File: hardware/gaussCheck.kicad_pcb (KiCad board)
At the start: 2 copper layers, 28 x 94.7 mm, 42 parts, among them J1 USB_C_Receptacle_USB2.0, J2 SWD, SW1 PTS810, SW2 CK KSC2, SW3 CK KSC2, SW4 CK KSC2, U1 TLV493D, U2 VIM-878-DP, U3 ATSAML22N18A-AUT, U4 TPS613221ADBV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

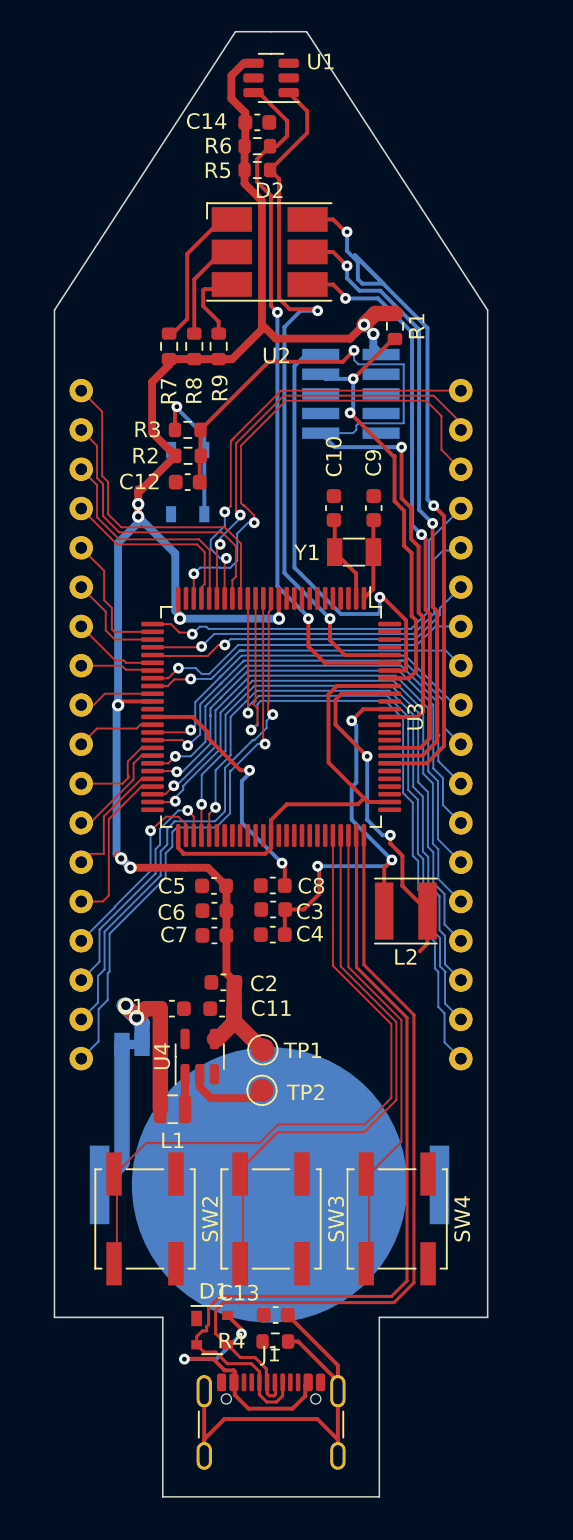
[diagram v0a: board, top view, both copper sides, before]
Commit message: Turned MCU by 45degress and rerouted
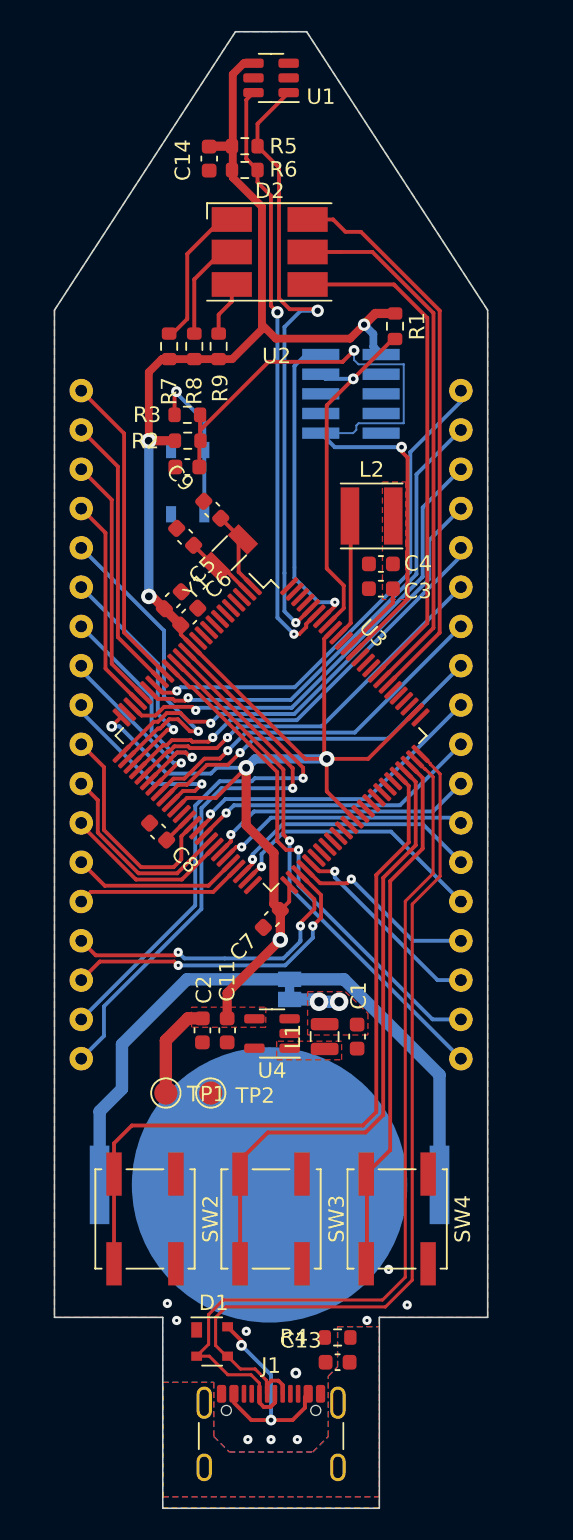
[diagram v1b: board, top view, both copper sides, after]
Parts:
- moved L2 25.6 mm to (106.5, 76.2), turned to 0 degrees
- moved C4 25.0 mm to (107.1, 79.3)
- moved C3 21.9 mm to (107.1, 80.9)
- moved C6 19.1 mm to (94.7, 82.7), turned to 45 degrees
- moved C5 18.7 mm to (93.7, 81.6), turned to 45 degrees
- moved C1 12.1 mm to (105.6, 109.8), turned to -90 degrees
- moved L1 10.9 mm to (103.5, 109.8), turned to -90 degrees
- moved JP1 10.8 mm to (101.2, 106.8), turned to -90 degrees
- moved C9 10.4 mm to (96.2, 75.8), turned to -45 degrees
- moved C10 9.79 mm to (94.4, 77.5), turned to -45 degrees
- moved C8 8.19 mm to (92.7, 96.6), turned to 135 degrees
- moved Y1 8.06 mm to (97.3, 78.6), turned to 45 degrees
- moved TP1 6.87 mm to (93.2, 113.5)
- moved C13 5.03 mm to (104.3, 130.9)
- moved U4 4.90 mm to (100.1, 109.7), turned to 180 degrees
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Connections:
- net /Bat renamed /BATT
- net /Bat_SW renamed /BATT_SW
- net Net-(U3D-VDDCORE) renamed /MCU/VDDCORE
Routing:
- net +BATT: track 9.68 -> 41.6 mm
- net Net-(J1-SHIELD): track 30.3 -> 0.00 mm
- net /MCU/DPCBA8: track 40.1 -> 13.0 mm
- net /MCU/MNGH8: track 38.6 -> 12.2 mm
- net /MCU/VDDCORE: track 27.9 -> 4.89 mm, vias 3 -> 0
- net /MCU/DPCBA7: track 36.5 -> 17.4 mm
- net /MCU/MNGH7: track 34.3 -> 16.9 mm
- net /MCU/DPCBA6: track 31.7 -> 16.4 mm
- net Net-(U3D-VLCD): track 16.7 -> 1.88 mm, vias 2 -> 0
- net Net-(U3D-VDDOUT): track 22.9 -> 8.07 mm, vias 2 -> 0
- net /MCU/LED1: track 48.9 -> 36.5 mm, vias 2 -> 0
- net /MCU/DEFCA3: track 8.79 -> 21.0 mm, vias 0 -> 1
- net /MCU/MNGH6: track 29.4 -> 17.7 mm
- net /MCU/COM2: track 44.3 -> 33.2 mm
- net /MCU/DEFCA4: track 5.58 -> 15.9 mm, vias 0 -> 1
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- added copper zone on F.Cu, net +3V3
- added copper zone on F.Cu, net /BATT
- added copper zone on F.Cu, net /BATT_SW
- added copper zone on F.Cu, net /MCU/VDDCORE
- added copper zone on B.Cu, net GND
- added copper zone on F.Cu, net GND
- added copper zone on B.Cu, net Net-(J1-SHIELD)
- added copper zone on F.Cu, net Net-(J1-SHIELD)
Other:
- board size 28 x 94.7 mm -> 28 x 95.4 mm

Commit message: 3v3 routing, change L2 to 0805 component
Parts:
- L2: footprint Inductor_SMD:L_Taiyo-Yuden_MD-4040 -> Inductor_SMD:L_0805_2012Metric
- moved L2 1.33 mm to (106.8, 77.5)
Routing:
- net +3V3: track 142.7 -> 147.3 mm
- net Net-(U3D-VDDOUT): track 8.07 -> 6.99 mm
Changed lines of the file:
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@@
     )
   )
-  (footprint "Inductor_SMD:L_Taiyo-Yuden_MD-4040" (layer "F.Cu")
-    (at 106.5 76.2)
-    (descr "Inductor, Taiyo Yuden, MD series, Taiyo-Yuden_MD-4040, 4.0mmx4.0mm")
-    (tags "inductor taiyo-yuden md smd")
-    (property "MPN" "LSXBD4040KKL100M")
+  (footprint "Inductor_SMD:L_0805_2012Metric" (layer "F.Cu")
+    (at 106.8 77.5)
+    (descr "Inductor SMD 0805 (2012 Metric), square (rectangular) end terminal, IPC_7351 nominal, (Body size source: IPC-SM-782 page 80, https://www.pcb-3d.com/wordpress/wp-content/uploads/ipc-sm-782a_amendment_1_and_2.pdf), generated with kicad-footprint-generator")
+    (tags "inductor")
+    (property "DCR" "650 mOhms")
+    (property "ISat" "200mA")
+    (property "MPN" "MLZ2012M100HT000")
     (property "Sheetfile" "gausCheck_MCU.kicad_sch")
     (property "Sheetname" "MCU")
@@
     (property "ki_keywords" "inductor choke coil reactor magnetic")
     (attr smd)
-    (fp_text reference "L2" (at 0 -3) (layer "F.SilkS")
-        (effects (font (size 1 1) (thickness 0.15)))
-    )
-    (fp_text value "10uH" (at 0 3.5) (layer "F.Fab")
+    (fp_text reference "L2" (at 0 -1.55) (layer "F.SilkS")
+        (effects (font (size 1 1) (thickness 0.15)))
+    )
+    (fp_text value "10uH" (at 0 1.55) (layer "F.Fab")
         (effects (font (size 1 1) (thickness 0.15)))
     )
     (fp_text user "${REFERENCE}" (at 0 0) (layer "F.Fab")
-        (effects (font (size 1 1) (thickness 0.15)))
-    )
-    (fp_line (start -2 -2.1) (end 2 -2.1)
-      (stroke (width 0.12) (type solid)) (layer "F.SilkS"))
-    (fp_line (start -2 2.1) (end 2 2.1)
-      (stroke (width 0.12) (type solid)) (layer "F.SilkS"))
-    (fp_line (start -2.25 -2.25) (end -2.25 2.25)
-      (stroke (width 0.05) (type solid)) (layer "F.CrtYd"))
-    (fp_line (start -2.25 2.25) (end 2.25 2.25)
-      (stroke (width 0.05) (type solid)) (layer "F.CrtYd"))
-    (fp_line (start 2.25 -2.25) (end -2.25 -2.25)
-      (stroke (width 0.05) (type solid)) (layer "F.CrtYd"))
-    (fp_line (start 2.25 2.25) (end 2.25 -2.25)
-      (stroke (width 0.05) (type solid)) (layer "F.CrtYd"))
-    (fp_line (start -2 -2) (end -2 2)
-      (stroke (width 0.1) (type solid)) (layer "F.Fab"))
-    (fp_line (start -2 2) (end 2 2)
-      (stroke (width 0.1) (type solid)) (layer "F.Fab"))
-    (fp_line (start 2 -2) (end -2 -2)
-      (stroke (width 0.1) (type solid)) (layer "F.Fab"))
-    (fp_line (start 2 2) (end 2 -2)
-      (stroke (width 0.1) (type solid)) (layer "F.Fab"))
-    (pad "1" smd rect (at -1.4 0) (size 1.2 3.7) (layers "F.Cu" "F.Paste" "F.Mask")
+        (effects (font (size 0.5 0.5) (thickness 0.08)))
+    )
+    (fp_line (start -0.399622 -0.56) (end 0.399622 -0.56)
+      (stroke (width 0.12) (type solid)) (layer "F.SilkS"))
+    (fp_line (start -0.399622 0.56) (end 0.399622 0.56)
+      (stroke (width 0.12) (type solid)) (layer "F.SilkS"))
+    (fp_line (start -1.75 -0.85) (end 1.75 -0.85)
+      (stroke (width 0.05) (type solid)) (layer "F.CrtYd"))
+    (fp_line (start -1.75 0.85) (end -1.75 -0.85)
+      (stroke (width 0.05) (type solid)) (layer "F.CrtYd"))
+    (fp_line (start 1.75 -0.85) (end 1.75 0.85)
+      (stroke (width 0.05) (type solid)) (layer "F.CrtYd"))
+    (fp_line (start 1.75 0.85) (end -1.75 0.85)
+      (stroke (width 0.05) (type solid)) (layer "F.CrtYd"))
+    (fp_line (start -1 -0.45) (end 1 -0.45)
+      (stroke (width 0.1) (type solid)) (layer "F.Fab"))
+    (fp_line (start -1 0.45) (end -1 -0.45)
+      (stroke (width 0.1) (type solid)) (layer "F.Fab"))
+    (fp_line (start 1 -0.45) (end 1 0.45)
+      (stroke (width 0.1) (type solid)) (layer "F.Fab"))
+    (fp_line (start 1 0.45) (end -1 0.45)
+      (stroke (width 0.1) (type solid)) (layer "F.Fab"))
+    (pad "1" smd roundrect (at -1.0625 0) (size 0.875 1.2) (layers "F.Cu" "F.Paste" "F.Mask") (roundrect_rratio 0.25)
       (net 42 "Net-(U3D-VDDOUT)") (pintype "passive"))
-    (pad "2" smd rect (at 1.4 0) (size 1.2 3.7) (layers "F.Cu" "F.Paste" "F.Mask")
+    (pad "2" smd roundrect (at 1.0625 0) (size 0.875 1.2) (layers "F.Cu" "F.Paste" "F.Mask") (roundrect_rratio 0.25)
       (net 107 "/MCU/VDDCORE") (pintype "passive"))
-    (model "${KICAD6_3DMODEL_DIR}/Inductor_SMD.3dshapes/L_Taiyo-Yuden_MD-4040.wrl"
+    (model "${KICAD6_3DMODEL_DIR}/Inductor_SMD.3dshapes/L_0805_2012Metric.wrl"
       (offset (xyz 0 0 0))
       (scale (xyz 1 1 1))
@@
   (via (at 101.6 131.6) (size 0.7) (drill 0.3) (layers "F.Cu" "B.Cu") (free) (net 2))
   (via (at 108.8 127.2) (size 0.6) (drill 0.2) (layers "F.Cu" "B.Cu") (free) (net 2))
-  (via (at 106.2 128.2) (size 0.6) (drill 0.2) (layers "F.Cu" "B.Cu") (free) (net 2))
+  (via (at 106.2 128) (size 0.6) (drill 0.2) (layers "F.Cu" "B.Cu") (free) (net 2))
   (segment (start 103.434585 91.734585) (end 103.434585 84.136988) (width 0.25) (layer "F.Cu") (net 3))
   (segment (start 92.087142 71.337142) (end 93.7875 71.337142) (width 0.6) (layer "F.Cu") (net 3))
@@
   (segment (start 98.390282 96.190282) (end 98.390282 92.474774) (width 0.6) (layer "F.Cu") (net 3))
   (segment (start 98.2375 46.937142) (end 97.525 47.649642) (width 0.508) (layer "F.Cu") (net 3))
+  (segment (start 97.8 86.1) (end 97.8 85.4) (width 0.6) (layer "F.Cu") (net 3))
   (segment (start 92.307968 81.4) (end 93.103984 82.196016) (width 0.6) (layer "F.Cu") (net 3))
   (segment (start 92.1 71.324284) (end 92.1 66.9) (width 0.508) (layer "F.Cu") (net 3))
@@
   (segment (start 106.278175 91.9) (end 109.307293 88.870882) (width 0.25) (layer "F.Cu") (net 3))
   (segment (start 101.175565 101.124435) (end 101.175565 100.060846) (width 0.25) (layer "F.Cu") (net 3))
-  (segment (start 102.207107 91.9) (end 94.935348 84.628241) (width 0.25) (layer "F.Cu") (net 3))
   (segment (start 103.434585 84.136988) (end 104.003992 83.567581) (width 0.25) (layer "F.Cu") (net 3))
   (segment (start 96.025358 52.299642) (end 96 52.325) (width 0.6) (layer "F.Cu") (net 3))
@@
   (segment (start 94.164644 83.857537) (end 94.935348 84.628241) (width 0.25) (layer "F.Cu") (net 3))
   (segment (start 96.440057 94.424999) (end 98.390282 92.474774) (width 0.25) (layer "F.Cu") (net 3))
+  (segment (start 103.6 91.9) (end 97.8 86.1) (width 0.6) (layer "F.Cu") (net 3))
   (segment (start 92.087142 71.337142) (end 92.1 71.324284) (width 0.508) (layer "F.Cu") (net 3))
   (segment (start 100.183582 97.983582) (end 98.390282 96.190282) (width 0.6) (layer "F.Cu") (net 3))
@@
   (segment (start 103.6 91.9) (end 103.6 94) (width 0.25) (layer "F.Cu") (net 3))
   (segment (start 106.0125 63.837142) (end 105.1125 64.737142) (width 0.508) (layer "F.Cu") (net 3))
-  (segment (start 103.6 91.9) (end 102.207107 91.9) (width 0.25) (layer "F.Cu") (net 3))
   (segment (start 93.103984 82.196016) (end 94.164644 83.256676) (width 0.6) (layer "F.Cu") (net 3))
   (segment (start 90.275565 89.224435) (end 89.7 89.8) (width 0.25) (layer "F.Cu") (net 3))
@@
   (via (at 106.0125 63.837142) (size 0.8) (drill 0.4) (layers "F.Cu" "B.Cu") (net 3))
   (via (at 92.1 81.4) (size 1) (drill 0.5) (layers "F.Cu" "B.Cu") (net 3))
-  (via (at 100.6 103.6) (size 1) (drill 0.5) (layers "F.Cu" "B.Cu") (net 3))
   (via (at 103.6 91.9) (size 1) (drill 0.5) (layers "F.Cu" "B.Cu") (net 3))
+  (via (at 97.8 85.4) (size 1) (drill 0.5) (layers "F.Cu" "B.Cu") (net 3))
   (via (at 98.390282 92.474774) (size 1) (drill 0.5) (layers "F.Cu" "B.Cu") (net 3))
   (segment (start 96.109187 92.85) (end 96.484413 92.474774) (width 0.25) (layer "B.Cu") (net 3))
   (segment (start 96.484413 92.474774) (end 98.390282 92.474774) (width 0.25) (layer "B.Cu") (net 3))
   (segment (start 90.2 89.8) (end 93.25 92.85) (width 0.25) (layer "B.Cu") (net 3))
+  (segment (start 96.1 85.4) (end 92.1 81.4) (width 0.6) (layer "B.Cu") (net 3))
   (segment (start 93.25 92.85) (end 96.109187 92.85) (width 0.25) (layer "B.Cu") (net 3))
   (segment (start 106.6125 64.437142) (end 106.6125 65.267142) (width 0.508) (layer "B.Cu") (net 3))
@@
   (segment (start 89.7 89.8) (end 90.2 89.8) (width 0.25) (layer "B.Cu") (net 3))
   (segment (start 106.6125 65.267142) (end 107.1125 65.767142) (width 0.508) (layer "B.Cu") (net 3))
+  (segment (start 97.8 85.4) (end 96.1 85.4) (width 0.6) (layer "B.Cu") (net 3))
   (segment (start 95.965 127.8168) (end 95.965 129.735) (width 0.2) (layer "F.Cu") (net 5))
   (segment (start 99.25 133.514999) (end 99.525001 133.79) (width 0.25) (layer "F.Cu") (net 5))
@@
   (segment (start 104.117943 71.752585) (end 103.2125 70.847142) (width 0.254) (layer "B.Cu") (net 41))
   (segment (start 105.3025 70.847142) (end 105.5125 70.637142) (width 0.125) (layer "B.Cu") (net 41))
-  (segment (start 105.147702 76.247702) (end 105.147702 83.130978) (width 0.25) (layer "F.Cu") (net 42))
-  (segment (start 105.1 76.2) (end 105.147702 76.247702) (width 0.25) (layer "F.Cu") (net 42))
   (segment (start 105.147702 83.130978) (end 104.357546 83.921134) (width 0.25) (layer "F.Cu") (net 42))
+  (segment (start 105.7375 77.5) (end 105.147702 78.089798) (width 0.25) (layer "F.Cu") (net 42))
+  (segment (start 105.147702 78.089798) (end 105.147702 83.130978) (width 0.25) (layer "F.Cu") (net 42))
   (segment (start 104.122702 82.034657) (end 104.122702 81.777298) (width 0.25) (layer "F.Cu") (net 45))
   (segment (start 103.296885 82.860474) (end 104.122702 82.034657) (width 0.25) (layer "F.Cu") (net 45))
@@
         (xy 108.7 81.6)
         (xy 107.2 81.6)
-        (xy 107.2 74)
-        (xy 108.7 74)
+        (xy 107.2 76.7)
+        (xy 108.7 76.7)
       )
     )

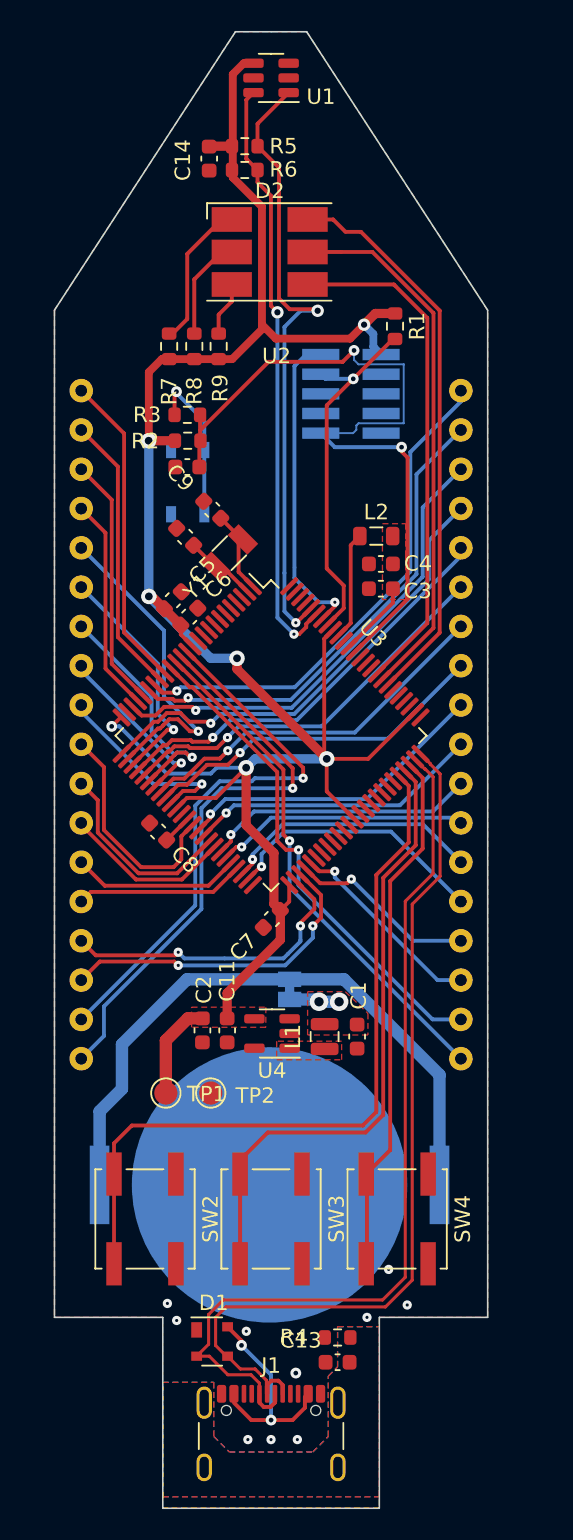
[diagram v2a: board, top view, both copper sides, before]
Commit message: via stitching, board outline, silkscreen
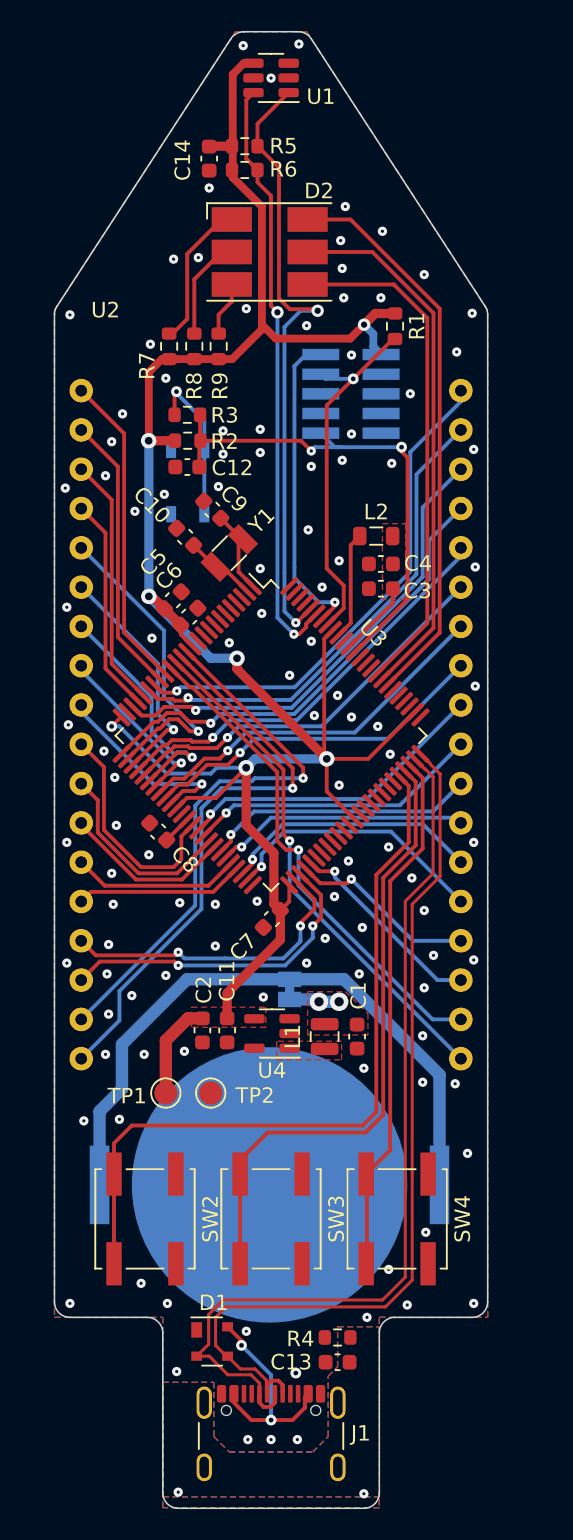
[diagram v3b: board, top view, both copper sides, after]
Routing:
- net /MCU/~{RESET}: track 49.6 -> 33.3 mm
- net Net-(J1-SHIELD): vias 0 -> 2
- net GND: vias 10 -> 112
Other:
- outline, holes or cut-outs redrawn
